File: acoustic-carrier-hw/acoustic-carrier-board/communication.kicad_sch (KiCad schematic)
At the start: 55 parts, among them IC1 ECP5-BGA256, J3 8P8C_Shielded, U1 KSZ9031RN, Y1 25MHz

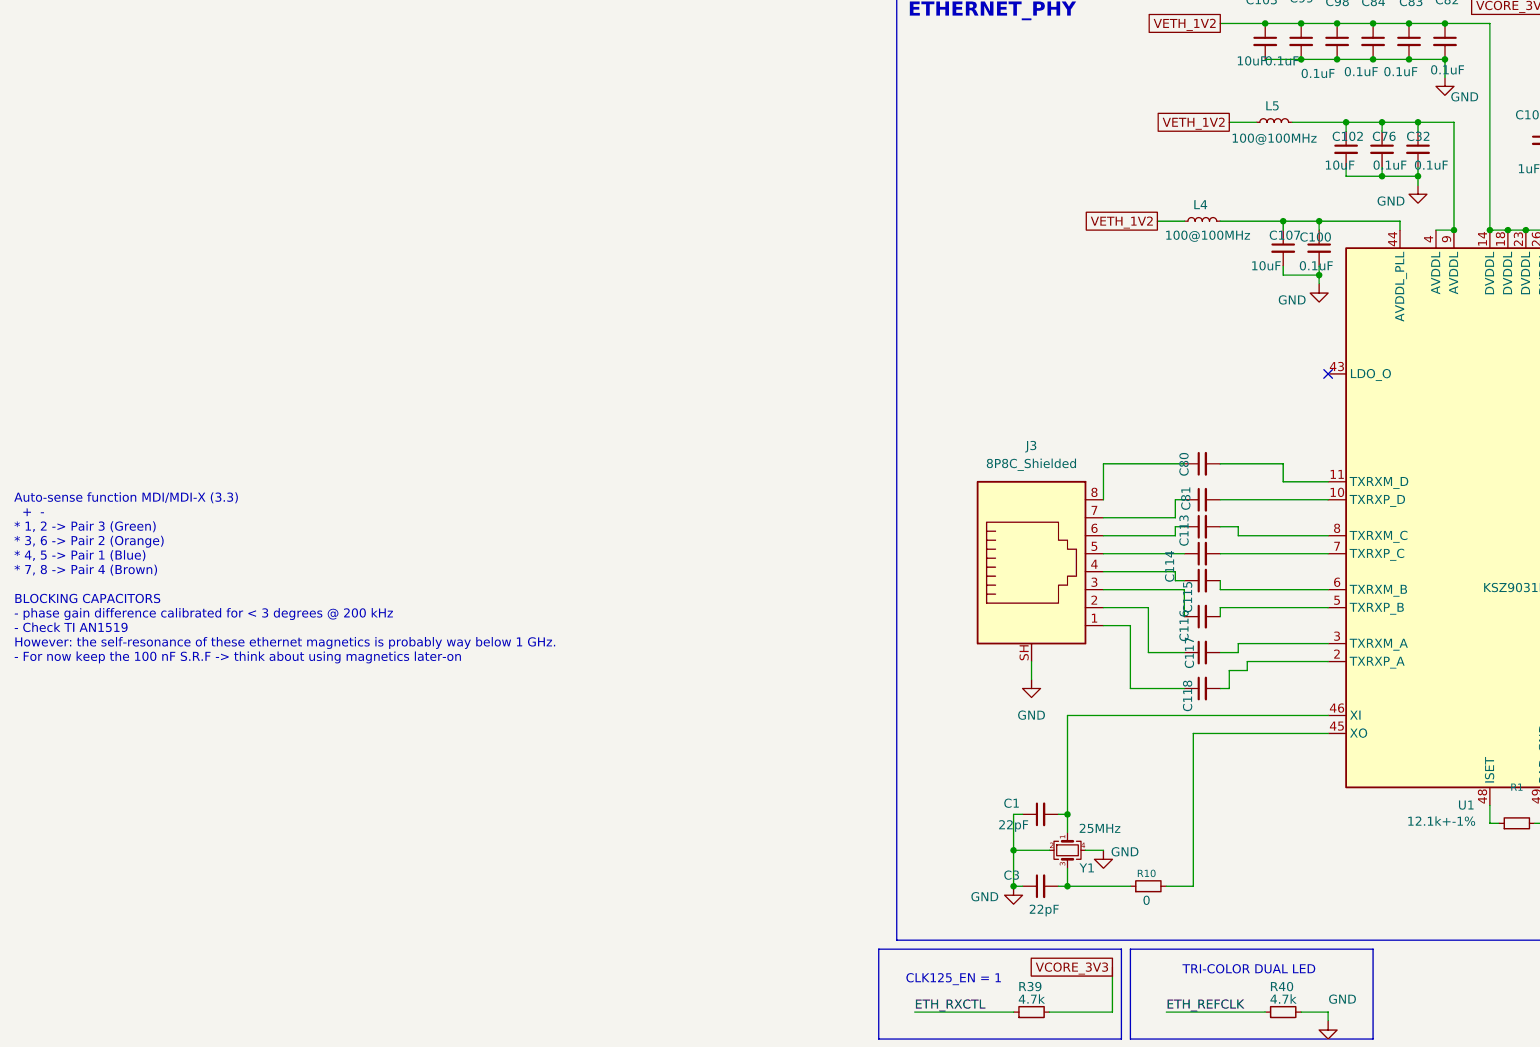
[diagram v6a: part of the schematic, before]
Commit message: [carrier] Added second adc input with magnetics, added ethernet connector with magnetics [piezodriver] Added diodes to level shifters for gate charge return current
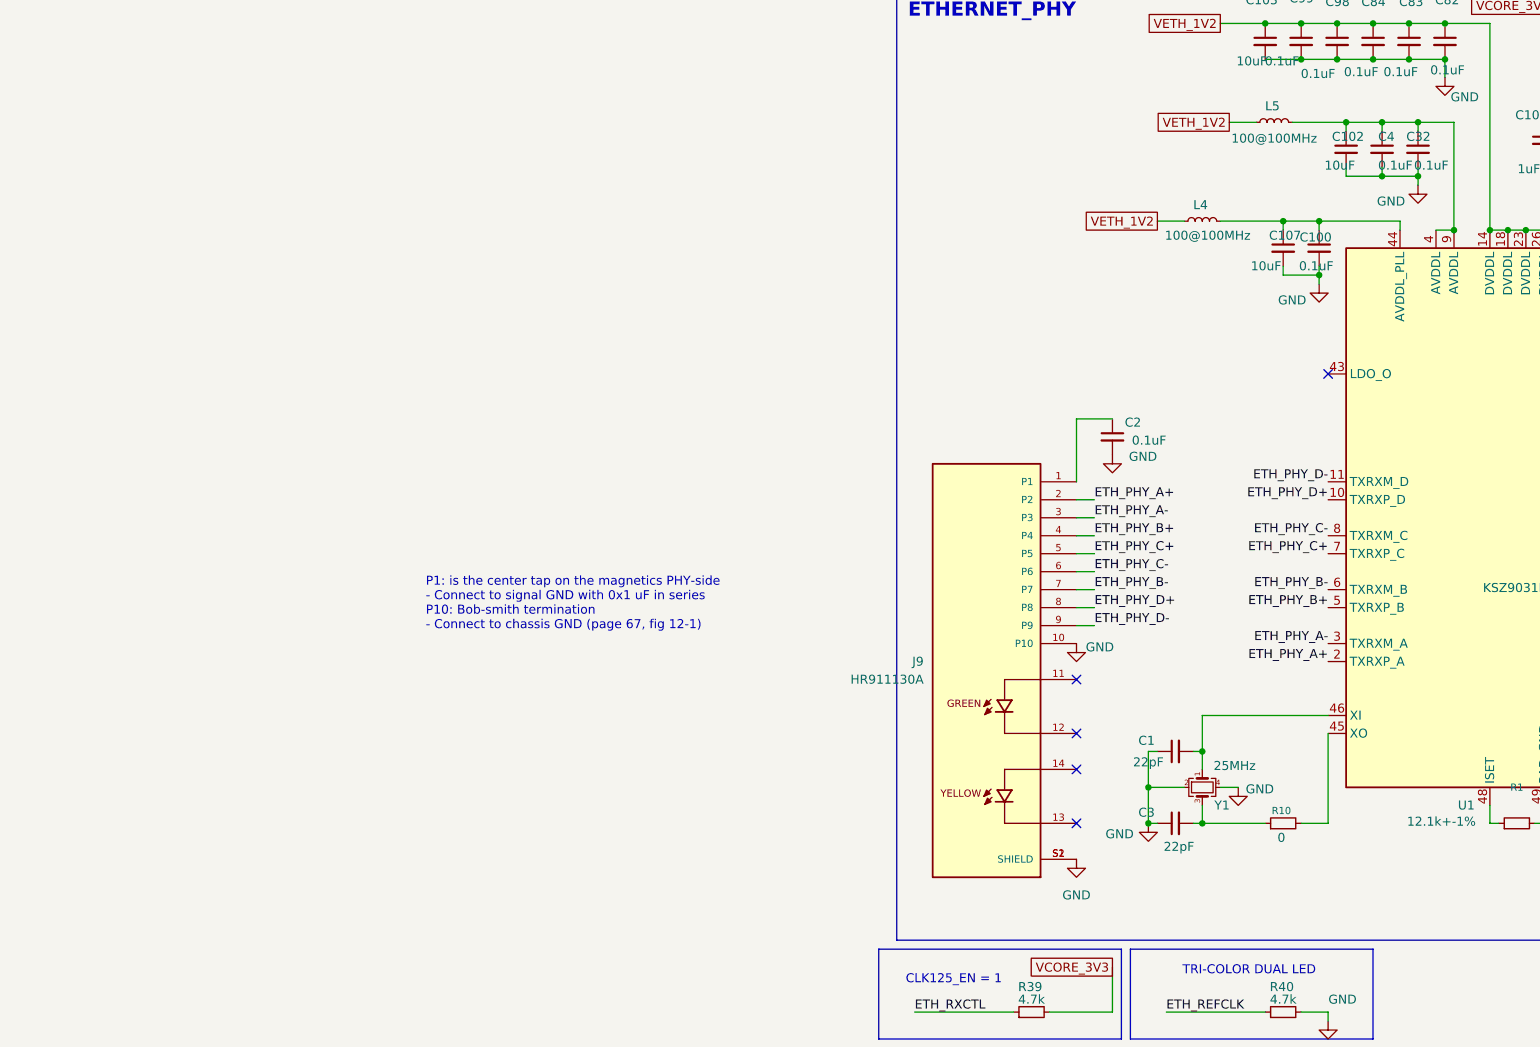
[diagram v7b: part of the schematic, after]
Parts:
- removed C113, C114, C115, C116, C117, C118, C80, C81: 100 nF +-5%, Capacitor_SMD:C_0603_1608Metric_Pad1.08x0.95mm_HandSolder, symbol Device:C_Small
- removed C76: 0.1uF, Capacitor_SMD:C_0402_1005Metric, symbol Device:C_Small
- removed J3: 8P8C_Shielded, Connector_RJ:RJ45_RCH_RC01937, symbol Connector:8P8C_Shielded
- added C2: 0.1uF, Capacitor_SMD:C_0603_1608Metric_Pad1.08x0.95mm_HandSolder, symbol Device:C_Small
- added C4: 0.1uF, Capacitor_SMD:C_0402_1005Metric, symbol Device:C_Small
- added J9: HR911130A, rj45:RJ45-TH_HR911130A, symbol RJ45_HR911130A:HR911130A
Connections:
- net GND: now also C2.2, C4.2, J9.10 (P10), J9.S1 (SHIELD), J9.S2 (SHIELD)
- net at C102.1, C32.1, L5.1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: now also C4.1
- net ETH_PHY_A-: now reaches U1.3 (TXRXM_A)
- net ETH_PHY_A-: now also J9.3 (P3)
- net ETH_PHY_D+: now reaches U1.10 (TXRXP_D)
- net ETH_PHY_D+: now also J9.8 (P8)
- net ETH_PHY_B+: now reaches U1.5 (TXRXP_B)
- net ETH_PHY_B+: now also J9.4 (P4)
- net ETH_PHY_C-: now reaches U1.8 (TXRXM_C)
- net ETH_PHY_C-: now also J9.6 (P6)
- net ETH_PHY_D-: now reaches U1.11 (TXRXM_D)
- net ETH_PHY_D-: now also J9.9 (P9)
- net ETH_PHY_A+: now reaches U1.2 (TXRXP_A)
- net ETH_PHY_A+: now also J9.2 (P2)
- net ETH_PHY_B-: now reaches U1.6 (TXRXM_B)
- net ETH_PHY_B-: now also J9.7 (P7)
- net ETH_PHY_C+: now reaches U1.7 (TXRXP_C)
- net ETH_PHY_C+: now also J9.5 (P5)
- new net: C2.1, J9.1 (P1)
- no-connect marks 1 -> 5
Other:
- note added: "P1: is the center tap on the magnetics PHY-side - Connect to signal GND with 0x1 uF in series P10: Bob-smith termination - Connect to chassis GND (page 67, fig 12-1)"
- note removed: "Auto-sense function MDI/MDI-X (3.3) + - * 1, 2 -> Pair 3 (Green) * 3, 6 -> Pair 2 (Orange) * 4, 5 -> Pair 1 (Blue) * 7, 8 -> Pair 4 (Brown) BLOCKING CAPACITORS - phase gain difference calibrated for < 3 degrees @ 200 kHz - Check TI AN1519 However: the self-resonance of these ethernet magnetics is probably way below 1 GHz. - For now keep the 100 nF S.R.F -> think about using magnetics later-on"
- moved on the sheet: C1, C3, R10, Y1

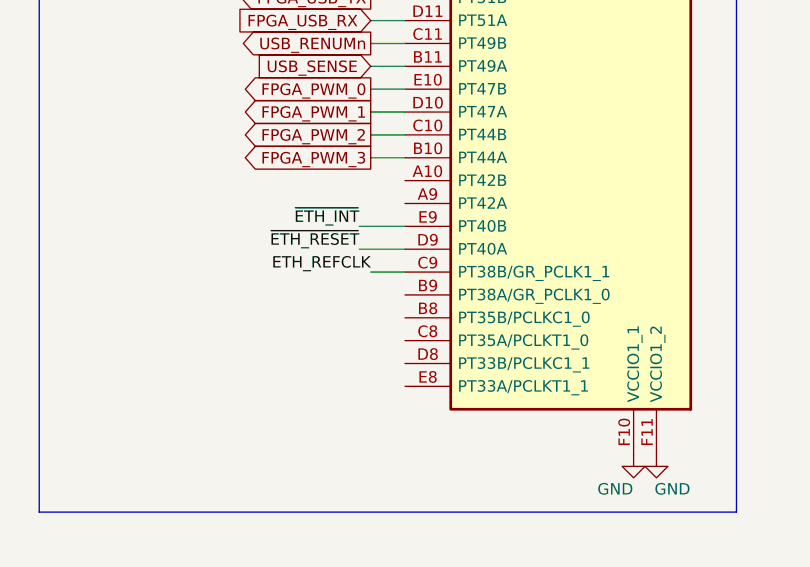
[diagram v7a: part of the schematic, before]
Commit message: [carrier] Started schematic check, replaced 8 with 16 pin connectors
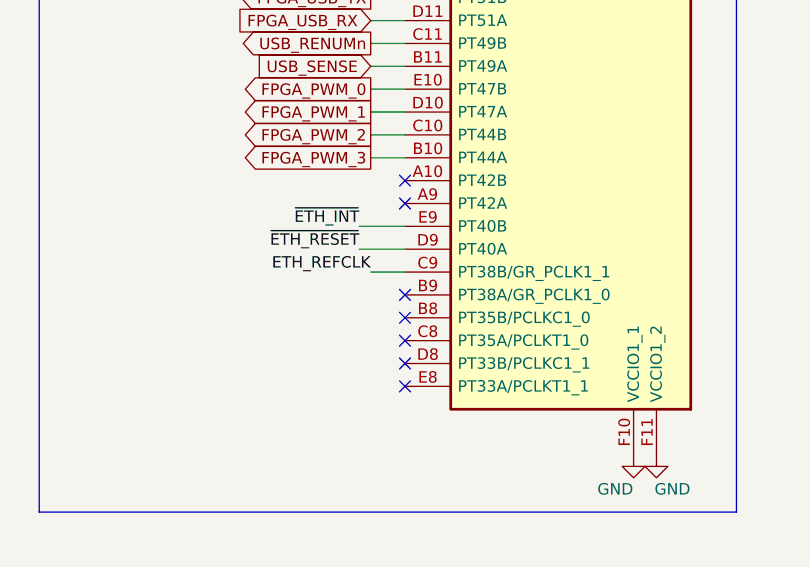
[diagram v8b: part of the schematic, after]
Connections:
- no-connect marks 5 -> 12
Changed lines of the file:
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@@
+	)
+	(no_connect
+		(at 234.95 92.71)
+	)
+	(no_connect
+		(at 234.95 102.87)
 	)
 	(no_connect
@@
 	)
 	(no_connect
+		(at 234.95 107.95)
+	)
+	(no_connect
+		(at 234.95 110.49)
+	)
+	(no_connect
+		(at 234.95 90.17)
+	)
+	(no_connect
 		(at 45.72 114.3)
+	)
+	(no_connect
+		(at 234.95 105.41)
 	)
 	(no_connect
@@
 		(at 81.28 71.12)
 	)
+	(no_connect
+		(at 234.95 113.03)
+	)
 	(wire
